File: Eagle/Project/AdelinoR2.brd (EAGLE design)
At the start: 47 x 53.3 mm, 80 parts, among them J1 DC-044-A, J2 YELLOW-8P-2.54, J3 YELLOW-6P-2.54, J4 YELLOW-8P-2.54, J5 YELLOW-8P-2.54, J6 4P-2.0, J7 YELLOW-2X3P-2.54, J8 4P-2.0, Q1 NCE3407A, Q2 CJ2305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

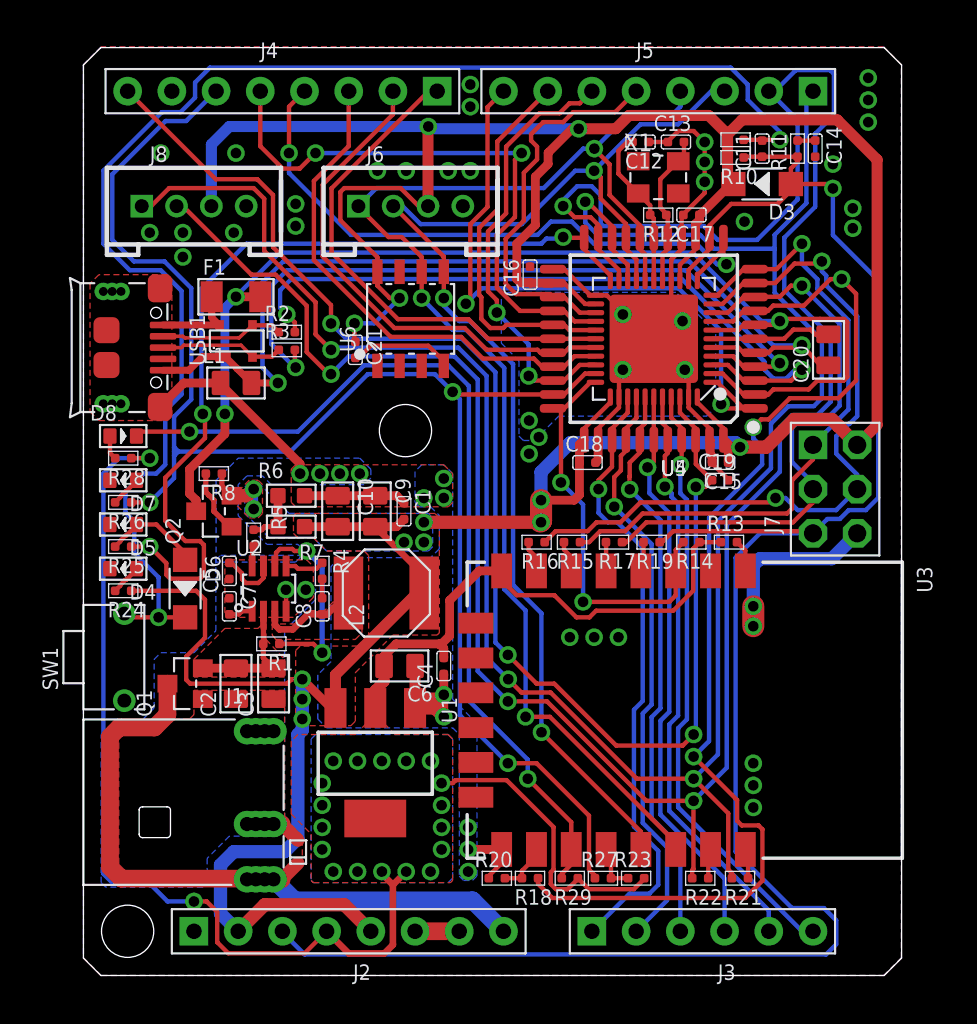
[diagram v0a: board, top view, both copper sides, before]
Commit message: Add 15V TVS from Shenzhen OPL.
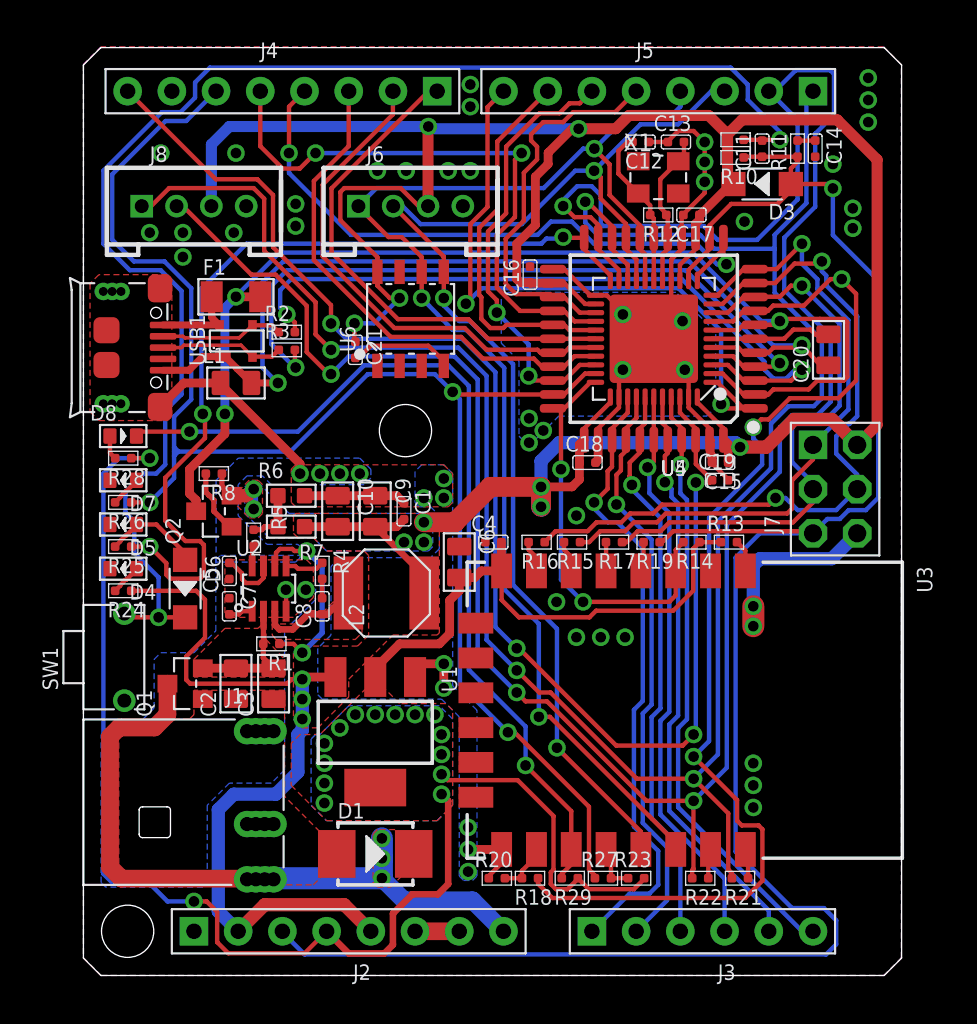
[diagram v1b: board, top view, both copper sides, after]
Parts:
- removed TVS1: (no value), Seeed-OPL-2017-01-Diode-james:SOD-523
- added D1: SMBJ15CA-13-F, Adelino-Misc:DO-214AA
- moved C4 7.66 mm to (23.5, 24.9), turned to 90 degrees
- moved C6 6.88 mm to (21.6, 23.7), turned to 0 degrees
- moved U1 1.78 mm to (16.8, 14.0)
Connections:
- net GND: now also D1.+; no longer TVS1.P$1
- net VIN: now also D1.-; no longer TVS1.P$2
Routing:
- net +5V: track 223.2 -> 214.5 mm
- net GND: track 101.9 -> 95.4 mm, vias 53 -> 55
- net +3V3: track 102.0 -> 107.8 mm, vias 20 -> 16
- net PIN_D13: track 91.8 -> 91.0 mm
- net SW_EN: track 11.6 -> 10.9 mm
- net PIN_D1: track 143.4 -> 142.8 mm
- net PIN_D0: track 129.0 -> 128.4 mm
- net VIN: track 41.0 -> 41.1 mm, vias 0 -> 3
- added copper zone on layer 1, net VIN

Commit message: Route 3.3V decoupling caps away from ESP-12F.
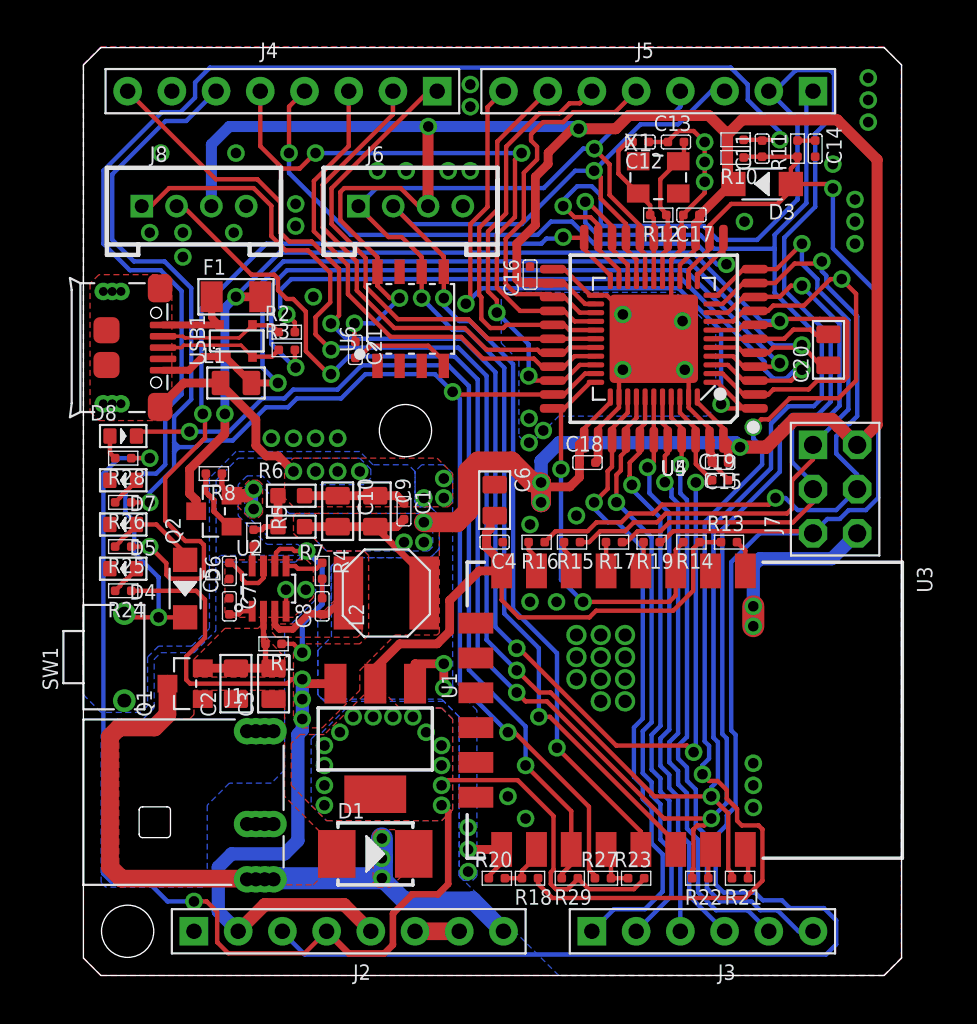
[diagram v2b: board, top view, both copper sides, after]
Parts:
- moved C6 4.10 mm to (23.6, 27.3)
- moved U1 0.38 mm to (16.8, 13.6)
- moved R1 0.13 mm to (10.9, 19.1)
- moved C4 0.08 mm to (23.6, 24.9), turned to 270 degrees
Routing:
- net RESET: track 112.8 -> 115.7 mm
- net +5V: track 214.5 -> 216.7 mm
- net PIN_D0: track 128.4 -> 130.6 mm
- net PIN_D1: track 142.8 -> 144.9 mm
- net PIN_AREF: track 80.4 -> 82.4 mm
- net PIN_A5: track 34.9 -> 36.7 mm
- net +3V3: track 107.8 -> 109.1 mm
- net PIN_A4: track 33.8 -> 34.8 mm
- net ACT_LED: track 50.6 -> 49.9 mm
- net PIN_A0: track 36.0 -> 36.6 mm
- net GND: track 95.4 -> 95.9 mm, vias 55 -> 73

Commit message: Added assembly placement.
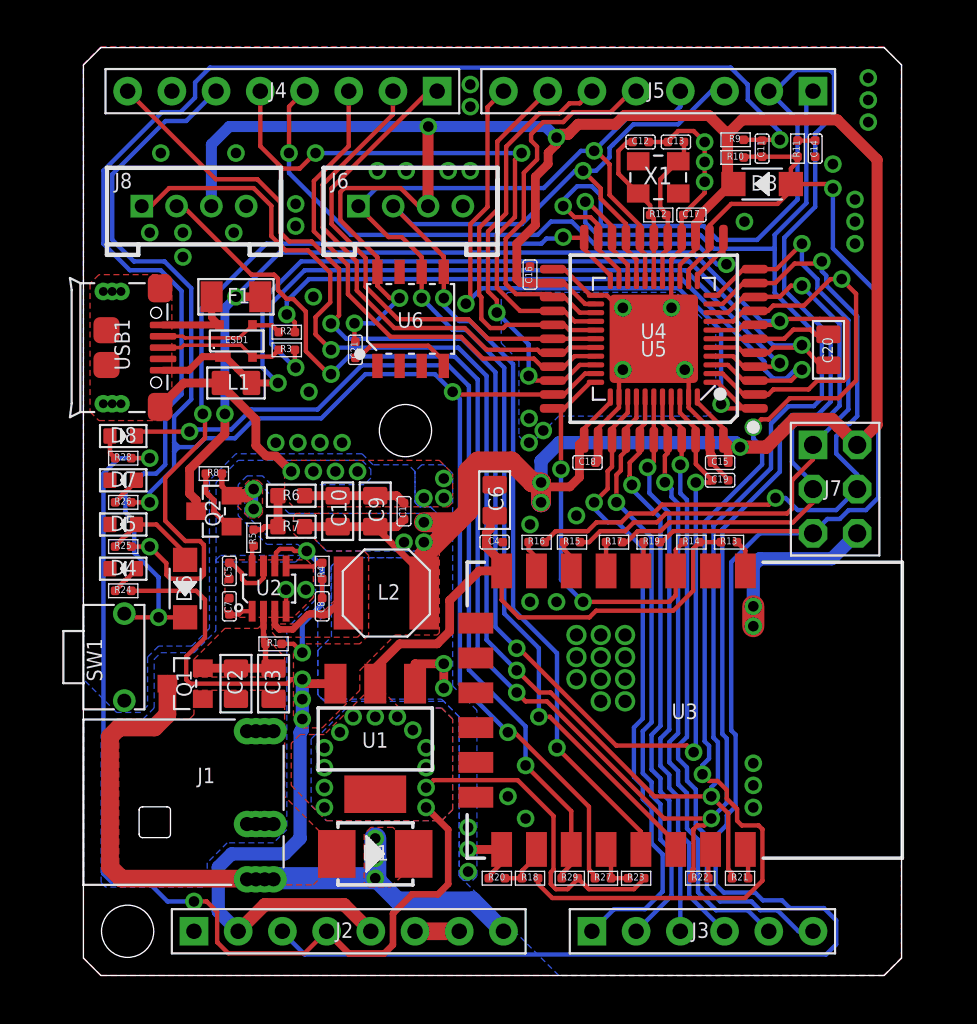
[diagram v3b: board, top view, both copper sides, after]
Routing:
- net +5V: track 216.7 -> 218.6 mm
- net +3V3: track 109.1 -> 110.2 mm, vias 16 -> 15
- net D-: track 41.6 -> 40.7 mm
- net UGND: track 54.7 -> 54.1 mm
- net D+: track 42.3 -> 41.7 mm
- net PIN_D2_SDA: track 73.1 -> 73.7 mm
- net GND: track 95.9 -> 95.5 mm, vias 73 -> 74
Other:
- board text added: "ESD1"

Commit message: Add DNP for 32U4 TQFP and ECC608; add some silk art for Adelino X2.
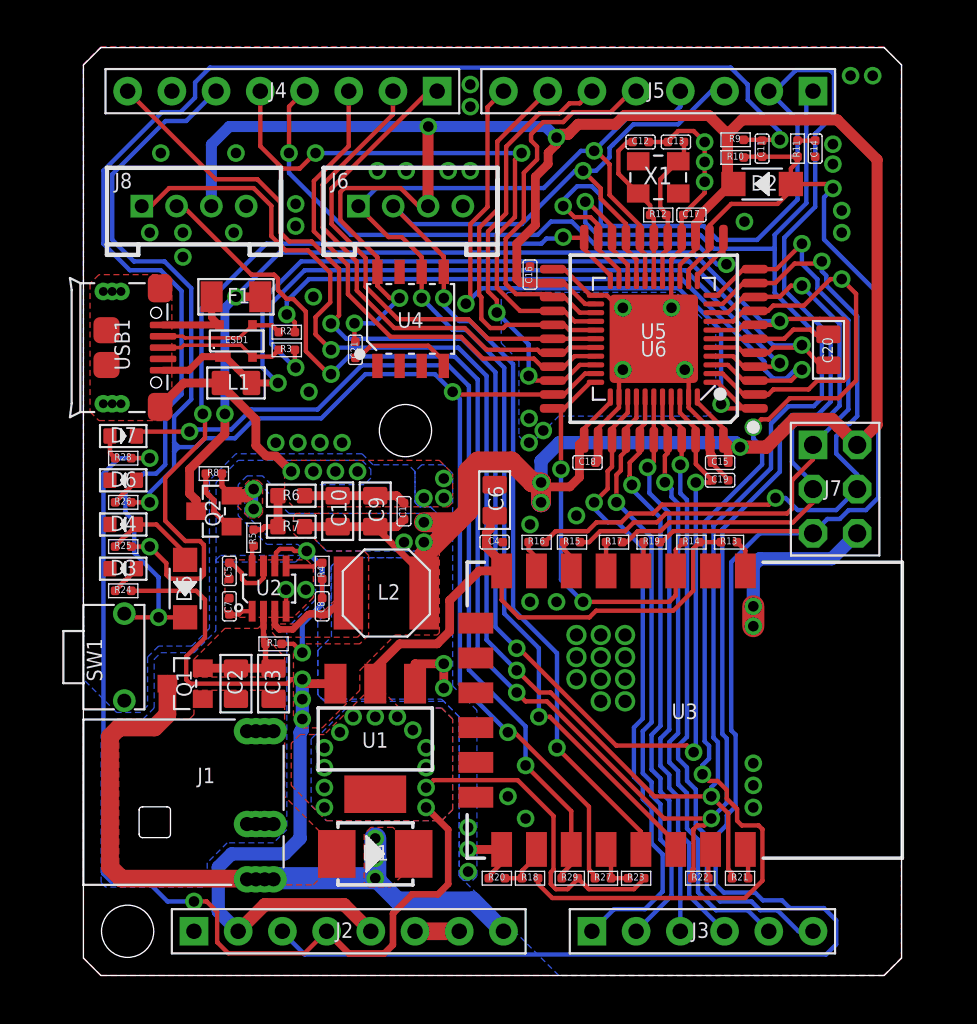
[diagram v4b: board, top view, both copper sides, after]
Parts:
- removed D8: BLU-0603, Seeed-LED:LED-0603
- added D2: 20V-500MA, Seeed-Diode:SOD-123
- D3: value 20V-500MA -> GRE-0603; device Seeed-Diode:SOD-123 -> Seeed-LED:LED-0603
- D4: value GRE-0603 -> YEL-0603
- D5: value YEL-0603 -> 20V-500MA; device Seeed-LED:LED-0603 -> Seeed-Diode:SOD-123
- D6: value 20V-500MA -> YEL-0603; device Seeed-Diode:SOD-123 -> Seeed-LED:LED-0603
- D7: value YEL-0603 -> BLU-0603
- U4: value ATMEGA32U4-MUR-QFN44 -> DNP; device Seeed-IC:QFN44G-0.5-7X7MM -> Adelino-Misc:SOIC8-1.27-5X4MM
- U5: value ATMEGA32U4-TQFP44 -> ATMEGA32U4-MUR-QFN44; device Seeed-IC:TQFP44-0.8-9.6X9.6MM -> Seeed-IC:QFN44G-0.5-7X7MM
- U6: value ATECC608-SOIC8 -> DNP; device Adelino-Misc:SOIC8-1.27-5X4MM -> Seeed-IC:TQFP44-0.8-9.6X9.6MM
- moved D3 42.8 mm to (2.29, 23.4)
- moved U4 14.0 mm to (18.8, 37.7), turned to 0 degrees
- moved U6 14.0 mm to (32.8, 36.6), turned to 180 degrees
- moved D6 7.17 mm to (2.29, 28.4), turned to 180 degrees
- moved D5 5.12 mm to (5.84, 22.2), turned to 270 degrees
- moved D4 2.54 mm to (2.29, 25.9)
- moved D7 2.54 mm to (2.29, 31.0), turned to 0 degrees
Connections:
- net +5V: now also D2.-, U4.8, U6.14, U6.24, U6.34, U6.44; no longer D3.-, U4.14, U4.24, U4.34, U4.44, U6.8
- net ACT_LED: now also U6.22; no longer U4.22
- net AT_MISO: now also U6.11; no longer U4.11
- net AT_MOSI: now also U6.10; no longer U4.10
- net AT_SCK: now also U6.9; no longer U4.9
- net AT_SS: now also U6.8; no longer U4.8
- net D+: now also U6.4; no longer U4.4
- net D-: now also U6.3; no longer U4.3
- net ESP_EN: now also U6.33; no longer U4.33
- net GND: now also D3.-, D6.-, U4.4, U5.TAB, U6.15, U6.23, U6.35, U6.43; no longer D5.-, D7.-, U4.15, U4.23, U4.35, U4.43, U4.TAB, U6.4
- net GPIO2_LED: now also D7.-; no longer D8.-
- net N$4: now also D7.+; no longer D8.+
- net PIN_A0: now also U6.36; no longer U4.36
- net PIN_A1: now also U6.37; no longer U4.37
- net PIN_A2: now also U6.38; no longer U4.38
- net PIN_A3: now also U6.39; no longer U4.39
- net PIN_A4: now also U6.40; no longer U4.40
- net PIN_A5: now also U6.41; no longer U4.41
- net PIN_AREF: now also U6.42; no longer U4.42
- net PIN_D0: now also U6.20; no longer U4.20
- net PIN_D1: now also U6.21; no longer U4.21
- net PIN_D10: now also U6.30; no longer U4.30
- net PIN_D11: now also U6.12; no longer U4.12
- net PIN_D12: now also U6.26; no longer U4.26
- net PIN_D13: now also U6.32; no longer U4.32
- net PIN_D2_SDA: now also U4.5, U6.19; no longer U4.19, U6.5
- net PIN_D3_SCL: now also U4.6, U6.18; no longer U4.18, U6.6
- net PIN_D4: now also U6.25; no longer U4.25
- net PIN_D5: now also U6.31; no longer U4.31
- net PIN_D6: now also U6.27; no longer U4.27
- net PIN_D7: now also U6.1; no longer U4.1
- net PIN_D8: now also U6.28; no longer U4.28
- net PIN_D9: now also U6.29; no longer U4.29
- net RESET: now also D2.+, U6.13; no longer D3.+, U4.13
- net RSTAT: now also D5.-; no longer D6.-
- net UCAP: now also U6.6; no longer U4.6
- net UGND: now also U6.5; no longer U4.5
- net VUSB: now also U6.2, U6.7; no longer U4.2, U4.7
- net XTAL1: now also U6.17; no longer U4.17
- net XTAL2: now also U6.16; no longer U4.16
- net _ACT: now also D4.+; no longer D6.+
- net _D13: now also D6.+; no longer D7.+
- net _PWR: now also D3.+; no longer D4.+
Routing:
- net GND: track 95.5 -> 95.2 mm, vias 74 -> 73
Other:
- board text added: "-GND-"
- board text added: "12"
- board text added: "2"
- board text added: "33"
- board text added: "4"
- board text added: "5V"
- board text added: "7"
- board text added: "8"
- board text added: "A0"
- board text added: "A1"
- board text added: "A2"
- board text added: "A3"
- board text added: "A4"
- board text added: "A5"
- board text added: "ACT"
- board text added: "ARF"
- board text added: "D13"
- board text added: "ESP"
- board text added: "GND"
- board text added: "ON"
- board text added: "RST"
- board text added: "RX0"
- board text added: "TX1"
- board text added: "VIN"
- board text added: "~10"
- board text added: "~11"
- board text added: "~13"
- board text added: "~3"
- board text added: "~5"
- board text added: "~6"
- board text added: "~9"

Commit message: Add Adelino X2 silkscreens and component position cues.
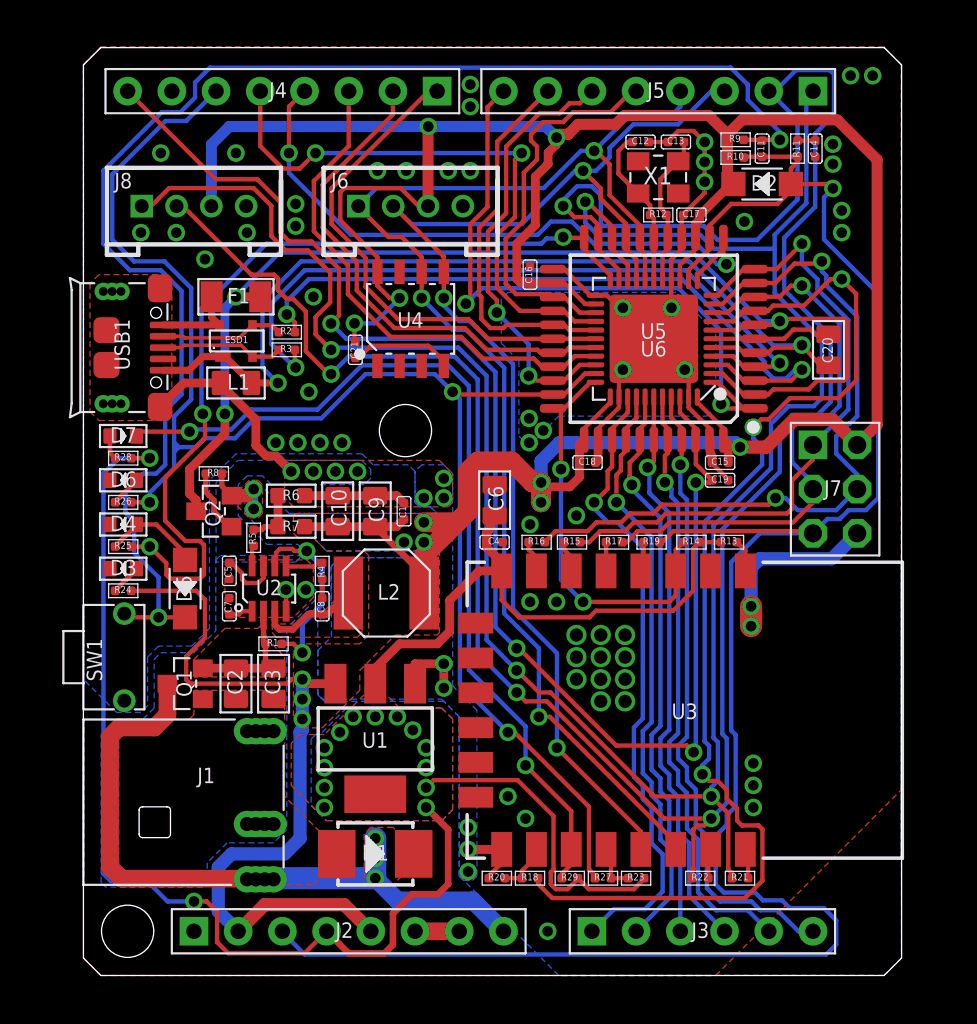
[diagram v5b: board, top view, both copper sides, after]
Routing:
- net GND: track 95.2 -> 93.3 mm, vias 73 -> 74
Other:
- board text added: "1"
- board text added: "33V"
- board text added: "Adelino X2 www.neoautus.com Product Validation"
- board text added: "ECC 608"
- board text added: "I2C"
- board text added: "ICSP"
- board text added: "R0"
- board text added: "RESET"
- board text added: "RX/TX"
- board text added: "SCL/SDA"
- board text added: "T1"
- board text added: "UART"
- board text added: "Vin"
- board text removed: "33"
- board text removed: "RX0"
- board text removed: "TX1"
- board text removed: "VIN"
